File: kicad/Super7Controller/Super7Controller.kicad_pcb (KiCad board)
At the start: 2 copper layers, 49.5 x 25.4 mm, 20 parts, among them P3 CONN_01X13, P4 CONN_01X09, U1 ULN2003A, U2 HiLetgo_ESP-WROOM-32_Developm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

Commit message: use new KiCad header instead of old one
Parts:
- P3: value CONN_01X13 -> Conn_01x13
- P4: value CONN_01X09 -> Conn_01x09
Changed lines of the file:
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@@
     (links 45)
     (no_connects 0)
-    (area 59.789287 46.83 118.820001 78.815001)
+    (area 69.139999 53.264999 118.820001 78.815001)
     (thickness 1.6)
     (drawings 8)
@@
       (effects (font (size 1 1) (thickness 0.15)) (justify mirror))
     )
-    (fp_text value CONN_01X13 (at 0 3.1 180) (layer B.Fab) hide
+    (fp_text value Conn_01x13 (at 0 3.1 180) (layer B.Fab) hide
       (effects (font (size 1 1) (thickness 0.15)) (justify mirror))
     )
@@
       (effects (font (size 1 1) (thickness 0.15)) (justify mirror))
     )
-    (fp_text value CONN_01X09 (at 0 3.1 180) (layer B.Fab) hide
-      (effects (font (size 1 1) (thickness 0.15)) (justify mirror))
-    )
+    (fp_text value Conn_01x09 (at 0 3.1 180) (layer B.Fab) hide
+      (effects (font (size 1 1) (thickness 0.15)) (justify mirror))
+    )

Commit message: Add silkscreen for ESP32 pin 1
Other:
- board text added: "Pin 1 ESP32 Board On This Side"
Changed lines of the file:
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@@
     (area 69.139999 53.264999 118.820001 78.815001)
     (thickness 1.6)
-    (drawings 8)
+    (drawings 9)
     (tracks 227)
     (zones 0)
@@
       (net 55 "Net-(U2-Pad19)"))
   )
+  (gr_text "Pin 1\nESP32 Board\nOn This Side" (at 72.8218 76.1238 90) (layer F.SilkS)
+    (effects (font (size 1 1) (thickness 0.2)) (justify left))
+  )
   (dimension 49.53 (width 0.3) (layer F.Fab)

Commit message: add silkscreen to ULN
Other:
- board text added: "ULN2003A"
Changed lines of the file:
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@@
     (links 45)
     (no_connects 0)
-    (area 69.139999 53.264999 118.820001 78.815001)
+    (area 59.789287 46.83 118.820001 78.815001)
     (thickness 1.6)
-    (drawings 9)
+    (drawings 12)
     (tracks 227)
     (zones 0)
@@
     (37 F.SilkS user)
     (38 B.Mask user)
-    (39 F.Mask user hide)
+    (39 F.Mask user)
     (40 Dwgs.User user)
     (41 Cmts.User user)
@@
       (net 55 "Net-(U2-Pad19)"))
   )
+  (gr_text ULN2003A (at 108 62.9 270) (layer B.SilkS)
+    (effects (font (size 1 1) (thickness 0.2)) (justify mirror))
+  )
+  (gr_circle (center 112.2934 58.4708) (end 112.3188 58.3692) (layer B.SilkS) (width 0.2))
+  (gr_circle (center 112.2934 58.4708) (end 112.395 58.1914) (layer B.SilkS) (width 0.2))
   (gr_text "Pin 1\nESP32 Board\nOn This Side" (at 72.8218 76.1238 90) (layer F.SilkS)
     (effects (font (size 1 1) (thickness 0.2)) (justify left))

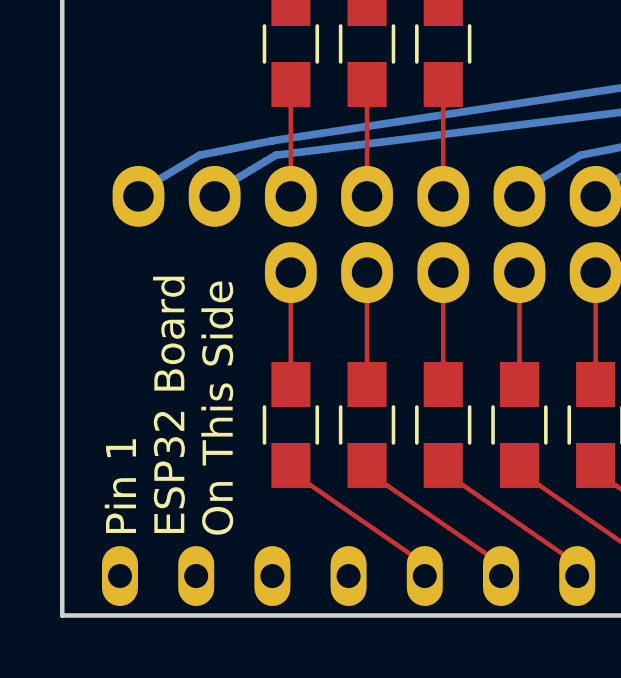
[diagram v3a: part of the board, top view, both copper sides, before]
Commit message: change and move text
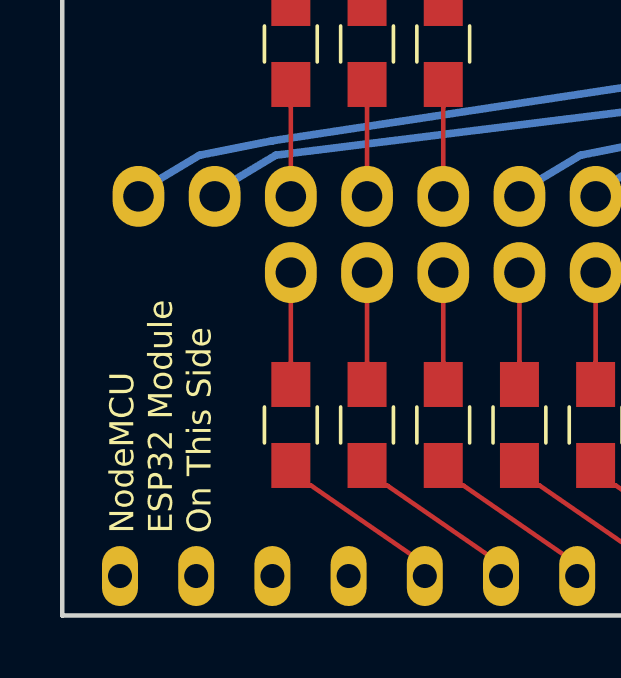
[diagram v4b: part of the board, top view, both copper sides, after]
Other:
- board text added: "NodeMCU ESP32 Module On This Side"
- board text removed: "Pin 1 ESP32 Board On This Side"
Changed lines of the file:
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@@
   (gr_circle (center 112.2934 58.4708) (end 112.3188 58.3692) (layer B.SilkS) (width 0.2))
   (gr_circle (center 112.2934 58.4708) (end 112.395 58.1914) (layer B.SilkS) (width 0.2))
-  (gr_text "Pin 1\nESP32 Board\nOn This Side" (at 72.8218 76.1238 90) (layer F.SilkS)
-    (effects (font (size 1 1) (thickness 0.2)) (justify left))
+  (gr_text "NodeMCU\nESP32 Module\nOn This Side" (at 72.5 76 90) (layer F.SilkS)
+    (effects (font (size 0.8 0.8) (thickness 0.2)) (justify left))
   )
   (dimension 49.53 (width 0.3) (layer F.Fab)

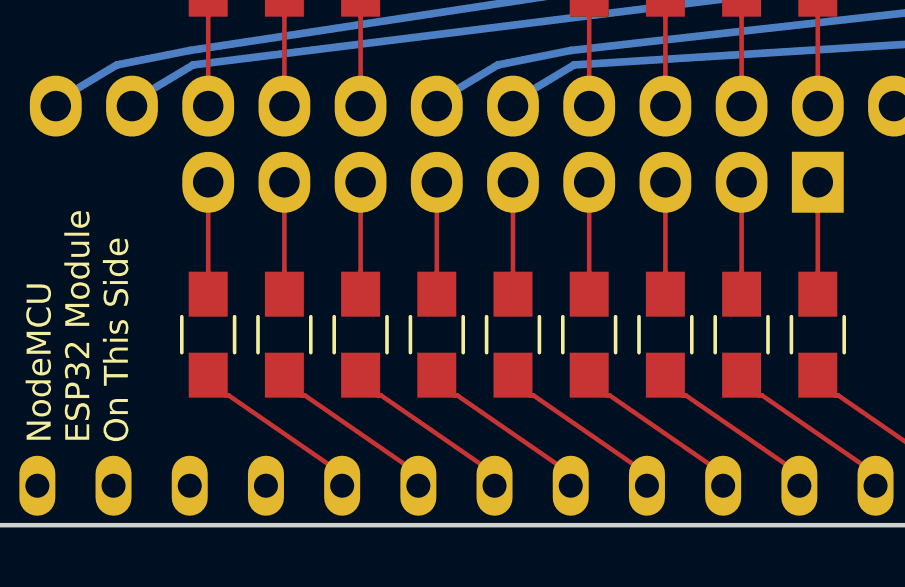
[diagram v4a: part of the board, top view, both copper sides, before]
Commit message: Apply bodge wire fix to controller PCB
Decimal points are no longer connected
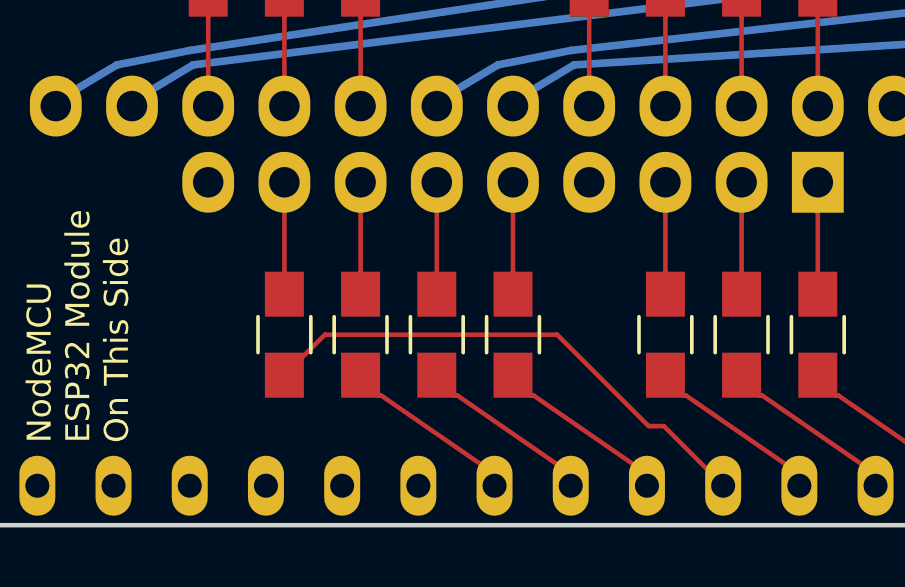
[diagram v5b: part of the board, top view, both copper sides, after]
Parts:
- removed R4, R9: 120, Resistors_SMD:R_0805_HandSoldering
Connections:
- P4 pad 4: H_DP1 -> (no net)
- P4 pad 9: H_DP2 -> (no net)
- U1 pad 10: Net-(U1-Pad10) -> (no net)
- U1 pad 7: Net-(U1-Pad7) -> (no net)
- U1 pad 9: Net-(U1-Pad9) -> (no net)
- U2 pad 1: VCC -> (no net)
- U2 pad 10: Net-(R4-Pad1) -> Net-(R8-Pad1)
- U2 pad 16: Net-(U2-Pad16) -> (no net)
- U2 pad 17: Net-(U2-Pad17) -> (no net)
- U2 pad 18: Net-(U2-Pad18) -> (no net)
- U2 pad 19: Net-(U2-Pad19) -> (no net)
- U2 pad 2: Net-(U2-Pad2) -> (no net)
- U2 pad 20: Net-(U2-Pad20) -> (no net)
- U2 pad 21: Net-(U2-Pad21) -> (no net)
- U2 pad 22: Net-(U2-Pad22) -> (no net)
- U2 pad 3: Net-(U2-Pad3) -> (no net)
- U2 pad 32: Net-(U2-Pad32) -> (no net)
- U2 pad 34: Net-(U2-Pad34) -> (no net)
- U2 pad 35: Net-(U2-Pad35) -> (no net)
- U2 pad 38: Net-(U2-Pad38) -> (no net)
- U2 pad 4: Net-(U2-Pad4) -> (no net)
- U2 pad 5: Net-(R9-Pad1) -> (no net)
- U2 pad 6: Net-(R8-Pad1) -> (no net)
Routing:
- net Net-(R8-Pad1): track 5.99 -> 18.6 mm
- net Net-(R9-Pad1): track 5.99 -> 0.00 mm
- net Net-(R4-Pad1): track 5.99 -> 0.00 mm
- net H_DP2: track 3.73 -> 0.00 mm
- net H_DP1: track 3.73 -> 0.00 mm
